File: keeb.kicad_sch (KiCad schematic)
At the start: 16 parts, among them SW1 SW_Push, U1 ATmega32U4-A, Y1 16MHz

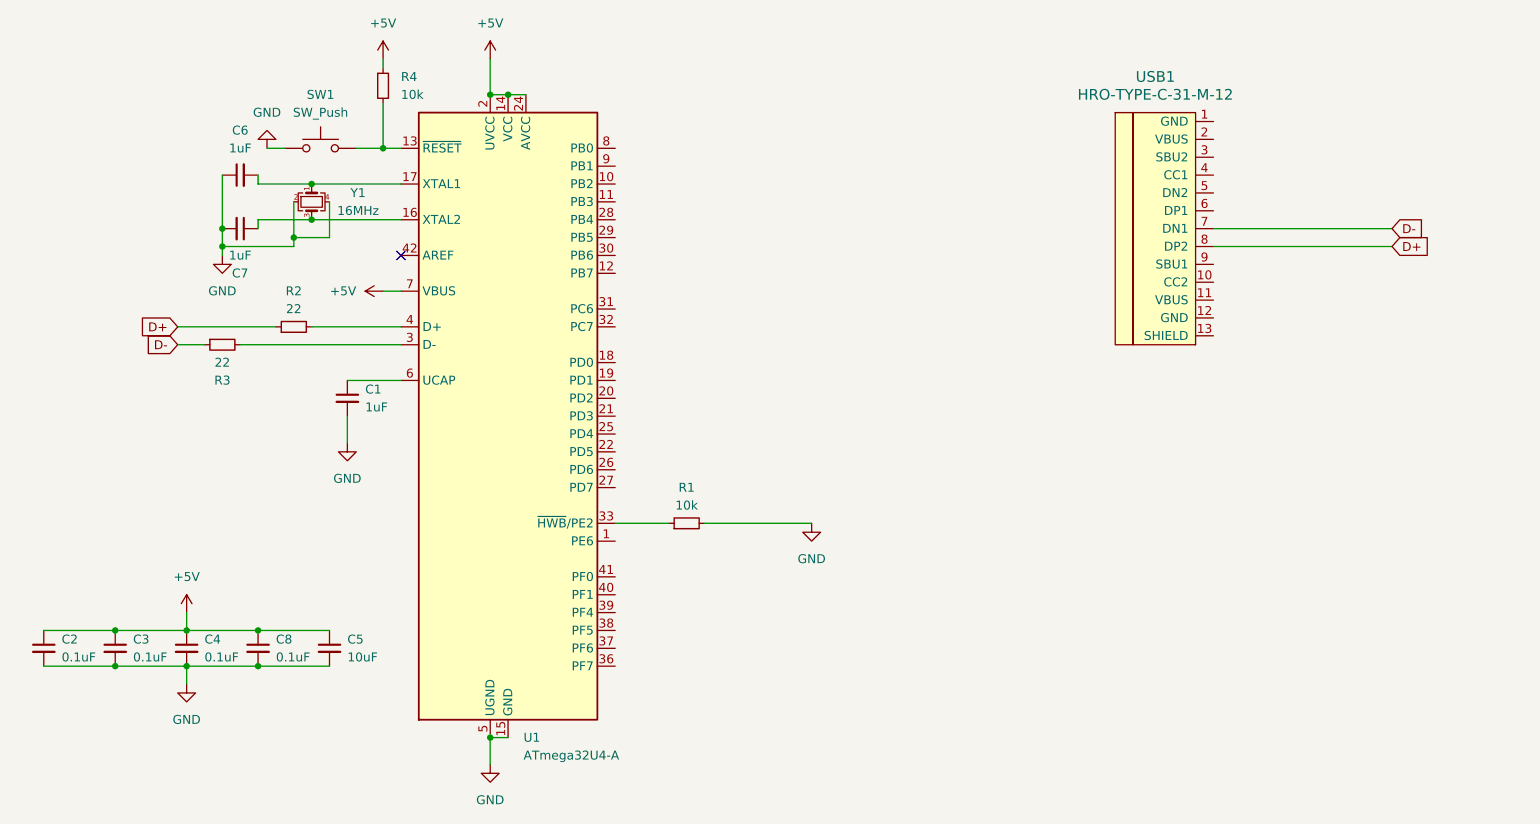
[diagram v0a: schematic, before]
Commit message: arcade session 2
usb c and matrix schematic done (with labels)
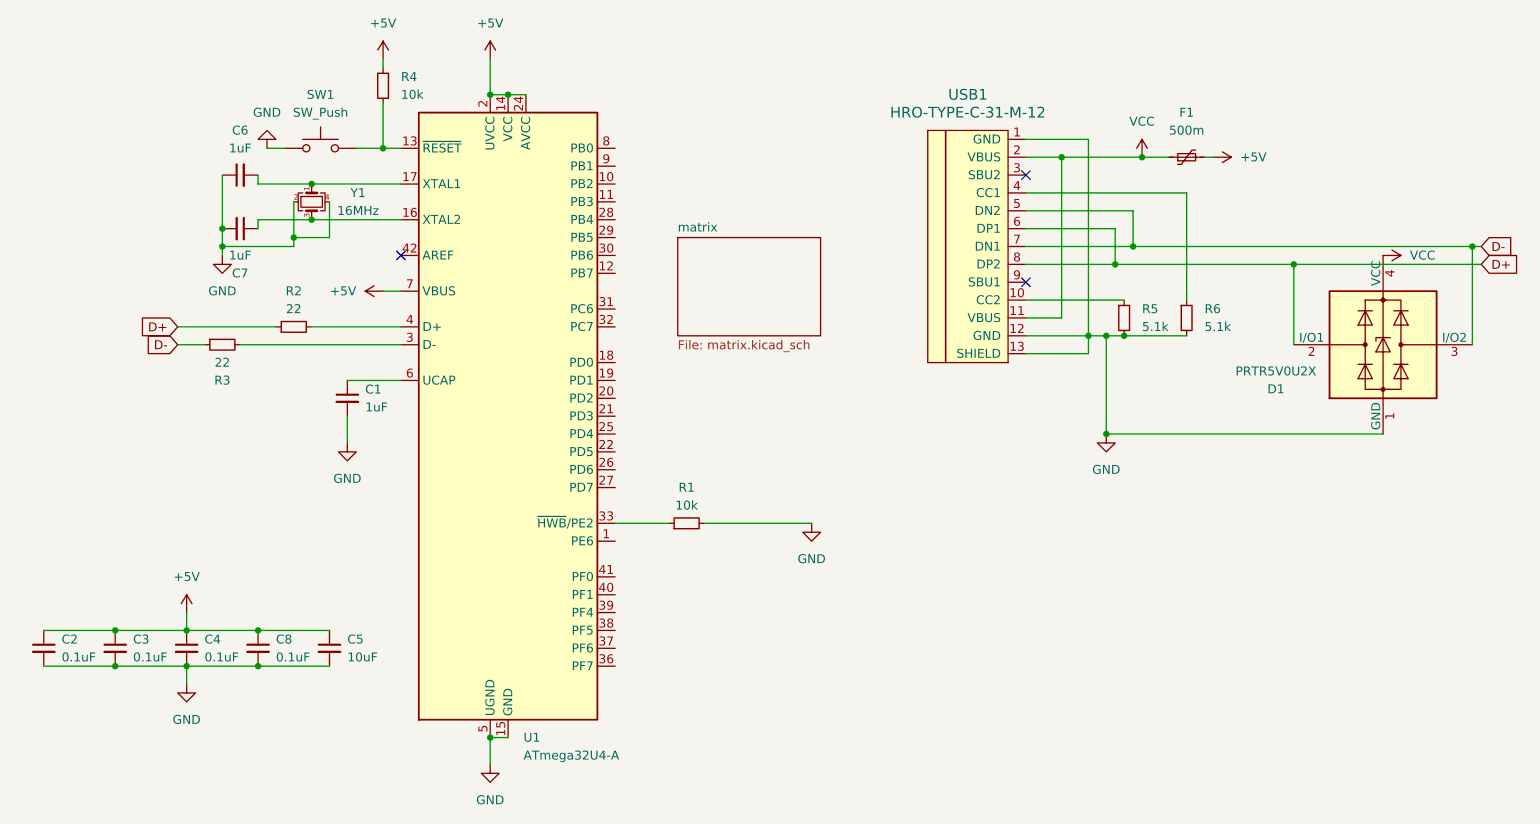
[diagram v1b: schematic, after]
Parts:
- added D1: PRTR5V0U2X, Package_TO_SOT_SMD:SOT-143, symbol Power_Protection:PRTR5V0U2X
- added F1: 500m, symbol Device:Polyfuse_Small
- added R5, R6: 5.1k, symbol Device:R_Small
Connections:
- net +5V: now also F1.2
- net D+: now also USB1.6 (DP1), D1.2 (I/O1)
- net D-: now also USB1.5 (DN2), D1.3 (I/O2)
- net GND: now also USB1.1 (GND), USB1.12 (GND), USB1.13 (SHIELD), D1.1 (GND), R5.2, R6.2
- net at USB1.10 (CC2): now also R5.1
- net VCC: now reaches USB1.11 (VBUS)
- net VCC: now also USB1.2 (VBUS), D1.4 (VCC), F1.1
- net at USB1.4 (CC1): now also R6.1
- no-connect marks 1 -> 3
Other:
- added sheet matrix (matrix.kicad_sch)
- moved on the sheet: USB1

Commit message: arcade session 3
added footprints; lots of errors :( problem for next time i am free
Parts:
- C1, C2, C3, C4, C5, C6, C7, C8: footprint (none) -> Capacitor_SMD:C_0805_2012Metric
- F1: footprint (none) -> Fuse:Fuse_1206_3216Metric_Pad1.42x1.75mm_HandSolder
- R1, R2, R3, R4, R5, R6: footprint (none) -> Resistor_SMD:R_0805_2012Metric
- SW1: footprint (none) -> Button_Switch_SMD:SW_SPST_SKQG_WithStem
- USB1: footprint (none) -> Type-C:Wurth-632723300011-HandSoldering
- Y1: footprint (none) -> Crystal:Crystal_SMD_3225-4Pin_3.2x2.5mm_HandSoldering
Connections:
- net row0: now reaches U1.1 (PE6)
- net col14: now reaches U1.11 (PB3)
- net col9: now reaches U1.18 (PD0)
- net col10: now reaches U1.19 (PD1)
- net col11: now reaches U1.20 (PD2)
- net col12: now reaches U1.21 (PD3)
- net col13: now reaches U1.22 (PD5)
- net col8: now reaches U1.25 (PD4)
- net col7: now reaches U1.26 (PD6)
- net col6: now reaches U1.27 (PD7)
- net col5: now reaches U1.28 (PB4)
- net col4: now reaches U1.29 (PB5)
- net col3: now reaches U1.30 (PB6)
- net col2: now reaches U1.31 (PC6)
- net col1: now reaches U1.32 (PC7)
- net col0: now reaches U1.36 (PF7)
- net row5: now reaches U1.37 (PF6)
- net row4: now reaches U1.38 (PF5)
- net row3: now reaches U1.39 (PF4)
- net row2: now reaches U1.40 (PF1)
- net row1: now reaches U1.41 (PF0)
- no-connect marks 3 -> 7

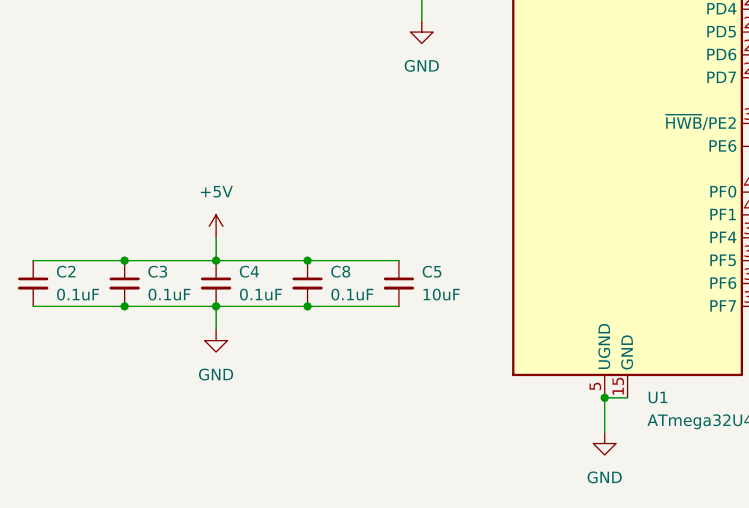
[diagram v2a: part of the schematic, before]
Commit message: arcade session 4(?)
footprints fixed and components placed/pcb editor settings set up
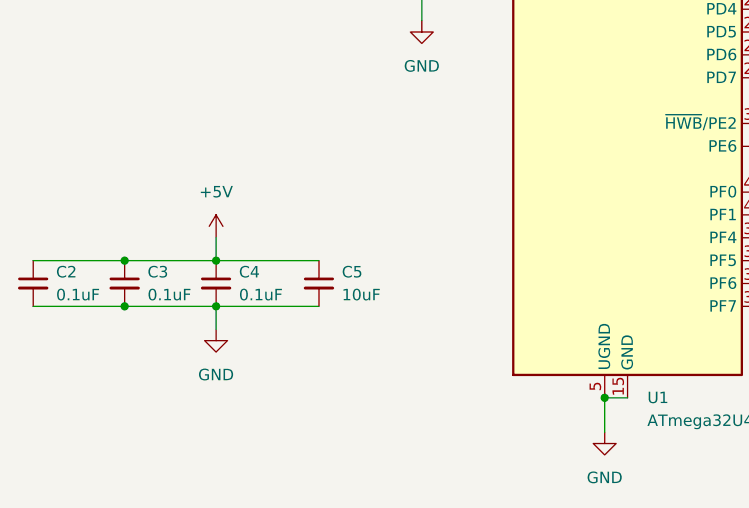
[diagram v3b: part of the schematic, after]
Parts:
- removed C8: 0.1uF, Capacitor_SMD:C_0805_2012Metric, symbol Device:C_Small
- USB1: footprint Type-C:Wurth-632723300011-HandSoldering -> Type-C:HRO-TYPE-C-31-M-12-HandSoldering
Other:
- moved on the sheet: C5
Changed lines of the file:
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@@
 	)
 	(junction
-		(at 49.53 104.14)
-		(diameter 0)
-		(color 0 0 0 0)
-	)
-	(junction
-		(at 49.53 109.22)
-		(diameter 0)
-		(color 0 0 0 0)
-	)
-	(junction
 		(at 173.99 49.53)
 		(diameter 0)
@@
 	(wire
 		(pts
-			(xy 39.37 104.14) (xy 49.53 104.14)
-		)
-		(stroke
-			(width 0)
-			(type default)
-		)
-	)
-	(wire
-		(pts
 			(xy 172.72 62.23) (xy 181.61 62.23)
 		)
@@
 	(wire
 		(pts
-			(xy 49.53 104.14) (xy 59.69 104.14)
+			(xy 39.37 104.14) (xy 50.8 104.14)
 		)
 		(stroke
@@
 	(wire
 		(pts
-			(xy 49.53 109.22) (xy 59.69 109.22)
+			(xy 39.37 109.22) (xy 50.8 109.22)
 		)
 		(stroke
@@
 	(wire
 		(pts
-			(xy 39.37 109.22) (xy 49.53 109.22)
-		)
-		(stroke
-			(width 0)
-			(type default)
-		)
-	)
-	(wire
-		(pts
 			(xy 67.31 29.21) (xy 67.31 35.56)
 		)
@@
 			)
 		)
-		(property "Footprint" "Type-C:Wurth-632723300011-HandSoldering"
+		(property "Footprint" "Type-C:HRO-TYPE-C-31-M-12-HandSoldering"
 			(at 156.21 48.26 0)
 			(effects
@@
 	)
 	(symbol
-		(lib_id "Device:C_Small")
-		(at 49.53 106.68 0)
-		(unit 1)
-		(exclude_from_sim no)
-		(in_bom yes)
-		(on_board yes)
-		(dnp no)
-		(fields_autoplaced yes)
-		(property "Reference" "C8"
-			(at 52.07 105.4162 0)
-			(effects
-				(font
-					(size 1.27 1.27)
-				)
-				(justify left)
-			)
-		)
-		(property "Value" "0.1uF"
-			(at 52.07 107.9562 0)
-			(effects
-				(font
-					(size 1.27 1.27)
-				)
-				(justify left)
-			)
-		)
-		(property "Footprint" "Capacitor_SMD:C_0805_2012Metric"
-			(at 49.53 106.68 0)
-			(effects
-				(font
-					(size 1.27 1.27)
-				)
-				(hide yes)
-			)
-		)
-		(property "Datasheet" "~"
-			(at 49.53 106.68 0)
-			(effects
-				(font
-					(size 1.27 1.27)
-				)
-				(hide yes)
-			)
-		)
-		(property "Description" "Unpolarized capacitor, small symbol"
-			(at 49.53 106.68 0)
-			(effects
-				(font
-					(size 1.27 1.27)
-				)
-				(hide yes)
-			)
-		)
-		(pin "2"
-		)
-		(pin "1"
-		)
-		(instances
-			(project "keeb"
-				(path "/30822975-2315-4055-85bb-b0314c985d97"
-					(reference "C8")
-					(unit 1)
-				)
-			)
-		)
-	)
-	(symbol
 		(lib_id "Device:R_Small")
 		(at 54.61 60.96 90)
@@
 	(symbol
 		(lib_id "Device:C_Small")
-		(at 59.69 106.68 0)
+		(at 50.8 106.68 0)
 		(unit 1)
 		(exclude_from_sim no)
@@
 		(fields_autoplaced yes)
 		(property "Reference" "C5"
-			(at 62.23 105.4162 0)
+			(at 53.34 105.4162 0)
 			(effects
 				(font
@@
 		)
 		(property "Value" "10uF"
-			(at 62.23 107.9562 0)
+			(at 53.34 107.9562 0)
 			(effects
 				(font
@@
 		)
 		(property "Footprint" "Capacitor_SMD:C_0805_2012Metric"
-			(at 59.69 106.68 0)
+			(at 50.8 106.68 0)
 			(effects
 				(font
@@
 		)
 		(property "Datasheet" "~"
-			(at 59.69 106.68 0)
+			(at 50.8 106.68 0)
 			(effects
 				(font
@@
 		)
 		(property "Description" "Unpolarized capacitor, small symbol"
-			(at 59.69 106.68 0)
+			(at 50.8 106.68 0)
 			(effects
 				(font

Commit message: fixed mistakes
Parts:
- added C8: 0.1uF, Capacitor_SMD:C_0805_2012Metric, symbol Device:C_Small
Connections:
- net +5V: now also C8.1
- net GND: now also C8.2
- net col0: now also U1.29 (PB5); no longer U1.36 (PF7)
- net col1: now also U1.30 (PB6); no longer U1.32 (PC7)
- net col3: now also U1.32 (PC7); no longer U1.30 (PB6)
- net col4: now also U1.36 (PF7); no longer U1.29 (PB5)
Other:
- moved on the sheet: C2, C3, C4, C5
